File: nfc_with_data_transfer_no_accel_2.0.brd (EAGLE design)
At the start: 13.2 x 18.4 mm, 7 parts

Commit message: fixed rst
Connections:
- net DOT1: now also MCU.6; no longer MCU.2
- net DOT5: now also MCU.1; no longer MCU.6
- net RST: now also MCU.2; no longer MCU.1
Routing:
- net DOT5: track 10.3 -> 0.00 mm
- net DOT1: track 3.30 -> 10.0 mm
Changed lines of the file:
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@@
 <layer number="14" name="Route14" color="1" fill="6" visible="no" active="no"/>
 <layer number="15" name="Route15" color="4" fill="6" visible="no" active="no"/>
-<layer number="16" name="Bottom" color="1" fill="1" visible="yes" active="yes"/>
+<layer number="16" name="Bottom" color="1" fill="1" visible="no" active="yes"/>
 <layer number="17" name="Pads" color="2" fill="1" visible="yes" active="yes"/>
 <layer number="18" name="Vias" color="2" fill="1" visible="yes" active="yes"/>
@@
 <contactref element="EINK" pad="5"/>
 <contactref element="MCU" pad="3"/>
+<wire x1="7.5946" y1="10.4394" x2="7.747" y2="10.287" width="0.3048" layer="1"/>
 <wire x1="8.5344" y1="7.6454" x2="8.5344" y2="8.6106" width="0.3048" layer="1"/>
-<wire x1="8.5344" y1="8.6106" x2="7.747" y2="9.398" width="0.3048" layer="1"/>
-<wire x1="7.747" y1="9.398" x2="7.747" y2="10.287" width="0.3048" layer="1"/>
-<wire x1="7.747" y1="10.287" x2="7.5946" y2="10.4394" width="0.3048" layer="1"/>
+<wire x1="8.5344" y1="8.6106" x2="7.62" y2="9.525" width="0.3048" layer="1"/>
+<wire x1="7.62" y1="9.525" x2="7.62" y2="10.414" width="0.3048" layer="1"/>
+<wire x1="7.62" y1="10.414" x2="7.5946" y2="10.4394" width="0.3048" layer="1"/>
 </signal>
 <signal name="DOT1">
 <contactref element="EINK" pad="3"/>
-<contactref element="MCU" pad="2"/>
-<wire x1="7.5438" y1="7.6454" x2="7.5438" y2="8.4582" width="0.3048" layer="1"/>
-<wire x1="7.5438" y1="8.4582" x2="6.35" y2="9.652" width="0.3048" layer="1"/>
-<wire x1="6.35" y1="9.652" x2="6.35" y2="10.414" width="0.3048" layer="1"/>
-<wire x1="6.35" y1="10.414" x2="6.3246" y2="10.4394" width="0.3048" layer="1"/>
+<contactref element="MCU" pad="6"/>
+<wire x1="7.5438" y1="7.6454" x2="7.5438" y2="8.3312" width="0.3048" layer="1"/>
+<wire x1="7.5438" y1="8.3312" x2="6.985" y2="8.89" width="0.3048" layer="1"/>
+<wire x1="6.985" y1="8.89" x2="6.985" y2="15.24" width="0.3048" layer="1"/>
+<wire x1="6.985" y1="15.24" x2="7.62" y2="15.875" width="0.3048" layer="1"/>
+<wire x1="7.62" y1="15.875" x2="7.62" y2="17.145" width="0.3048" layer="1"/>
+<wire x1="7.62" y1="17.145" x2="7.5946" y2="17.1704" width="0.3048" layer="1"/>
 </signal>
 <signal name="RST">
 <contactref element="EINK" pad="1"/>
-<contactref element="MCU" pad="1"/>
 <wire x1="6.5278" y1="7.9502" x2="6.5278" y2="7.6454" width="0.3048" layer="1"/>
-<wire x1="6.5278" y1="7.6454" x2="6.5278" y2="8.0772" width="0.3048" layer="1"/>
 <wire x1="5.08" y1="9.525" x2="5.08" y2="10.414" width="0.3048" layer="1"/>
-<wire x1="5.08" y1="10.414" x2="5.0546" y2="10.4394" width="0.3048" layer="1"/>
-<wire x1="6.5278" y1="7.6454" x2="6.5278" y2="8.0772" width="0.3048" layer="1"/>
-<wire x1="6.5278" y1="8.0772" x2="5.08" y2="9.525" width="0.3048" layer="1"/>
+<contactref element="MCU" pad="2"/>
+<wire x1="6.5278" y1="7.6454" x2="6.5278" y2="10.2362" width="0.3048" layer="1"/>
+<wire x1="6.5278" y1="10.2362" x2="6.3246" y2="10.4394" width="0.3048" layer="1"/>
+<wire x1="6.3246" y1="10.4394" x2="5.08" y2="10.414" width="0" layer="19" extent="1-1"/>
 </signal>
 <signal name="2.8V">
@@
 <signal name="DOT5">
 <contactref element="EINK" pad="7"/>
-<contactref element="MCU" pad="6"/>
-<wire x1="9.525" y1="11.557" x2="9.525" y2="7.6454" width="0.3048" layer="1"/>
-<wire x1="7.5946" y1="17.1704" x2="7.5946" y2="13.4874" width="0.3048" layer="1"/>
-<wire x1="7.5946" y1="13.4874" x2="9.525" y2="11.557" width="0.3048" layer="1"/>
+<contactref element="MCU" pad="1"/>
+<wire x1="5.0546" y1="10.4394" x2="9.525" y2="7.6454" width="0" layer="19" extent="1-1"/>
 </signal>
 </signals>

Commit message: final
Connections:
- removed net DOT3: EINK.5, MCU.3
- net DOT1: now also MCU.3; no longer MCU.6
- net DOT5: now also MCU.6; no longer MCU.1
- net GND: now also EINK.5
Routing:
- net GND: track 18.5 -> 32.1 mm
- net DOT5: track 0.00 -> 10.3 mm
- net DOT1: track 10.0 -> 2.82 mm
- net DOT3: track 3.40 -> 0.00 mm
- net RST: track 4.07 -> 3.18 mm
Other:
- board text added: "AlterNail"
- board text added: "RevB"
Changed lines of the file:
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@@
 <dimension x1="16.891" y1="2.032128125" x2="16.891" y2="20.32" x3="20.828" y3="11.1760625" textsize="1.778" layer="47"/>
 <dimension x1="16.891" y1="20.32" x2="3.683" y2="20.32" x3="10.287" y3="22.225" textsize="1.778" layer="47"/>
+<text x="11.557" y="6.096" size="1.27" layer="16" font="vector" ratio="20" rot="MR90">AlterNail</text>
+<text x="9.271" y="6.223" size="1.27" layer="16" font="vector" ratio="20" rot="MR90">RevB</text>
 </plain>
 <attributes>
@@
 </elements>
 <signals>
-<signal name="DOT3">
-<contactref element="EINK" pad="5"/>
-<contactref element="MCU" pad="3"/>
-<wire x1="7.5946" y1="10.4394" x2="7.747" y2="10.287" width="0.3048" layer="1"/>
-<wire x1="8.5344" y1="7.6454" x2="8.5344" y2="8.6106" width="0.3048" layer="1"/>
-<wire x1="8.5344" y1="8.6106" x2="7.62" y2="9.525" width="0.3048" layer="1"/>
-<wire x1="7.62" y1="9.525" x2="7.62" y2="10.414" width="0.3048" layer="1"/>
-<wire x1="7.62" y1="10.414" x2="7.5946" y2="10.4394" width="0.3048" layer="1"/>
-</signal>
 <signal name="DOT1">
 <contactref element="EINK" pad="3"/>
-<contactref element="MCU" pad="6"/>
-<wire x1="7.5438" y1="7.6454" x2="7.5438" y2="8.3312" width="0.3048" layer="1"/>
-<wire x1="7.5438" y1="8.3312" x2="6.985" y2="8.89" width="0.3048" layer="1"/>
-<wire x1="6.985" y1="8.89" x2="6.985" y2="15.24" width="0.3048" layer="1"/>
-<wire x1="6.985" y1="15.24" x2="7.62" y2="15.875" width="0.3048" layer="1"/>
-<wire x1="7.62" y1="15.875" x2="7.62" y2="17.145" width="0.3048" layer="1"/>
-<wire x1="7.62" y1="17.145" x2="7.5946" y2="17.1704" width="0.3048" layer="1"/>
+<contactref element="MCU" pad="3"/>
+<wire x1="7.5438" y1="7.6454" x2="7.5438" y2="10.3886" width="0.3048" layer="1"/>
+<wire x1="7.5438" y1="10.3886" x2="7.5946" y2="10.4394" width="0.3048" layer="1"/>
 </signal>
 <signal name="RST">
 <contactref element="EINK" pad="1"/>
 <wire x1="6.5278" y1="7.9502" x2="6.5278" y2="7.6454" width="0.3048" layer="1"/>
-<wire x1="5.08" y1="9.525" x2="5.08" y2="10.414" width="0.3048" layer="1"/>
 <contactref element="MCU" pad="2"/>
-<wire x1="6.5278" y1="7.6454" x2="6.5278" y2="10.2362" width="0.3048" layer="1"/>
-<wire x1="6.5278" y1="10.2362" x2="6.3246" y2="10.4394" width="0.3048" layer="1"/>
-<wire x1="6.3246" y1="10.4394" x2="5.08" y2="10.414" width="0" layer="19" extent="1-1"/>
+<wire x1="6.5278" y1="7.6454" x2="6.5278" y2="8.7122" width="0.3048" layer="1"/>
+<wire x1="6.5278" y1="8.7122" x2="6.35" y2="8.89" width="0.3048" layer="1"/>
+<wire x1="6.35" y1="8.89" x2="6.35" y2="10.414" width="0.3048" layer="1"/>
+<wire x1="6.35" y1="10.414" x2="6.3246" y2="10.4394" width="0.3048" layer="1"/>
 </signal>
 <signal name="2.8V">
@@
 <contactref element="C1" pad="1"/>
 <wire x1="15.3322" y1="13.5434" x2="15.3322" y2="14.1934" width="0.3048" layer="1"/>
-<wire x1="15.3322" y1="13.5434" x2="15.9206" y2="13.5434" width="0.3048" layer="1"/>
-<wire x1="15.9206" y1="13.5434" x2="16.383" y2="13.081" width="0.3048" layer="1"/>
-<wire x1="16.383" y1="13.081" x2="16.383" y2="10.795" width="0.3048" layer="1"/>
-<wire x1="16.383" y1="10.795" x2="15.113" y2="9.525" width="0.3048" layer="1"/>
+<wire x1="15.3322" y1="13.5434" x2="15.7936" y2="13.5434" width="0.3048" layer="1"/>
+<wire x1="15.7936" y1="13.5434" x2="16.002" y2="13.335" width="0.3048" layer="1"/>
+<wire x1="16.002" y1="13.335" x2="16.002" y2="10.414" width="0.3048" layer="1"/>
+<wire x1="16.002" y1="10.414" x2="15.113" y2="9.525" width="0.3048" layer="1"/>
 <wire x1="15.113" y1="9.525" x2="14.6186" y2="9.525" width="0.3048" layer="1"/>
 <wire x1="14.6186" y1="9.525" x2="14.5288" y2="9.6148" width="0.3048" layer="1"/>
@@
 <contactref element="R5" pad="1"/>
 <wire x1="12.827" y1="11.3148" x2="12.7" y2="11.176" width="0.3048" layer="1"/>
-<wire x1="11.4756" y1="13.5434" x2="10.9822" y2="13.5434" width="0.3048" layer="1"/>
 <wire x1="11.4756" y1="13.5434" x2="12.827" y2="12.192" width="0.3048" layer="1"/>
 <wire x1="12.827" y1="12.192" x2="12.827" y2="11.3148" width="0.3048" layer="1"/>
-<wire x1="6.3246" y1="17.1704" x2="6.3246" y2="18.2626" width="0.3048" layer="1"/>
-<wire x1="6.3246" y1="18.2626" x2="6.604" y2="18.542" width="0.3048" layer="1"/>
-<wire x1="8.2296" y1="18.288" x2="8.2296" y2="15.24" width="0.3048" layer="1"/>
+<wire x1="6.3246" y1="17.1704" x2="6.3246" y2="18.288" width="0.3048" layer="1"/>
+<wire x1="6.3246" y1="18.288" x2="6.604" y2="18.5928" width="0.3048" layer="1"/>
+<wire x1="8.2296" y1="15.24" x2="8.2296" y2="18.3134" width="0.3048" layer="1"/>
+<wire x1="6.604" y1="18.5928" x2="7.9502" y2="18.5928" width="0.3048" layer="1"/>
+<wire x1="7.9502" y1="18.5928" x2="8.2296" y2="18.3134" width="0.3048" layer="1"/>
 <wire x1="10.9822" y1="13.5434" x2="9.9516" y2="13.5434" width="0.3048" layer="1"/>
-<wire x1="9.9516" y1="13.5434" x2="8.2296" y2="15.24" width="0.3048" layer="1"/>
-<wire x1="6.604" y1="18.542" x2="7.9756" y2="18.542" width="0.3048" layer="1"/>
-<wire x1="7.9756" y1="18.542" x2="8.2296" y2="18.288" width="0.3048" layer="1"/>
+<wire x1="11.4756" y1="13.5434" x2="10.9822" y2="13.5434" width="0.3048" layer="1"/>
+<wire x1="8.2296" y1="15.24" x2="9.9516" y2="13.5434" width="0.3048" layer="1"/>
 </signal>
 <signal name="COIL">
@@
 <contactref element="MCU" pad="4"/>
 <contactref element="C1" pad="2"/>
-<polygon width="0.3048" layer="1">
+<polygon width="0.3048" layer="1" rank="2">
 <vertex x="17.653" y="19.558"/>
 <vertex x="3.048" y="19.558"/>
@@
 <vertex x="17.653" y="2.286"/>
 </polygon>
-<wire x1="8.0264" y1="6.7056" x2="8.0264" y2="7.6454" width="0.3048" layer="1"/>
-<wire x1="8.0264" y1="6.7056" x2="8.128" y2="6.604" width="0.3048" layer="1"/>
-<wire x1="9.0424" y1="6.6294" x2="9.0424" y2="7.6454" width="0.3048" layer="1"/>
-<wire x1="9.0424" y1="6.6294" x2="9.017" y2="6.604" width="0.3048" layer="1"/>
 <wire x1="11.4524" y1="17.7038" x2="10.9982" y2="17.7038" width="0.3048" layer="1"/>
 <wire x1="10.9982" y1="17.7038" x2="9.525" y2="19.05" width="0.3048" layer="1"/>
 <wire x1="9.525" y1="19.05" x2="6.223" y2="19.05" width="0.3048" layer="1"/>
-<wire x1="6.223" y1="19.05" x2="5.715" y2="18.542" width="0.3048" layer="1"/>
-<wire x1="5.715" y1="18.542" x2="5.715" y2="15.367" width="0.3048" layer="1"/>
-<wire x1="5.715" y1="15.367" x2="5.588" y2="15.24" width="0.3048" layer="1"/>
+<wire x1="6.223" y1="19.05" x2="5.6896" y2="18.4912" width="0.3048" layer="1"/>
+<wire x1="5.6896" y1="18.4912" x2="5.6896" y2="15.3162" width="0.3048" layer="1"/>
+<wire x1="5.6896" y1="15.3162" x2="5.588" y2="15.24" width="0.3048" layer="1"/>
 <wire x1="10.9822" y1="14.1934" x2="10.5716" y2="14.1934" width="0.3048" layer="1"/>
 <wire x1="10.5716" y1="14.1934" x2="9.906" y2="14.859" width="0.3048" layer="1"/>
@@
 <wire x1="9.906" y1="14.859" x2="9.906" y2="12.573" width="0.3048" layer="16"/>
 <via x="9.906" y="12.573" extent="1-16" drill="0.6" shape="octagon"/>
-<wire x1="9.0424" y1="7.6454" x2="9.0424" y2="10.2616" width="0.3048" layer="1"/>
-<wire x1="9.0424" y1="10.2616" x2="8.8646" y2="10.4394" width="0.3048" layer="1"/>
-<wire x1="10.9982" y1="17.7038" x2="9.906" y2="14.859" width="0" layer="19" extent="1-1"/>
+<contactref element="EINK" pad="5"/>
+<wire x1="9.0424" y1="6.4516" x2="8.5344" y2="6.4516" width="0.3048" layer="1"/>
+<wire x1="8.0264" y1="6.5278" x2="8.0264" y2="7.6454" width="0.3048" layer="1"/>
+<wire x1="8.0264" y1="6.5278" x2="8.5344" y2="6.5278" width="0.3048" layer="1"/>
+<wire x1="8.5344" y1="6.5278" x2="8.5344" y2="6.4516" width="0.3048" layer="1"/>
+<wire x1="8.5344" y1="8.7376" x2="8.5344" y2="6.5278" width="0.3048" layer="1"/>
+<wire x1="8.5344" y1="8.7376" x2="9.0424" y2="8.7376" width="0.3048" layer="1"/>
+<wire x1="9.0424" y1="8.7376" x2="9.0424" y2="8.763" width="0.3048" layer="1"/>
+<wire x1="9.0424" y1="8.7376" x2="9.0424" y2="7.6454" width="0.3048" layer="1"/>
+<wire x1="9.0424" y1="7.6454" x2="9.0424" y2="6.4516" width="0.3048" layer="1"/>
+<wire x1="8.0264" y1="7.6454" x2="8.0264" y2="8.8392" width="0.3048" layer="1"/>
+<wire x1="8.0264" y1="8.8392" x2="8.5344" y2="8.8392" width="0.3048" layer="1"/>
+<wire x1="8.5344" y1="8.8392" x2="8.5344" y2="8.7376" width="0.3048" layer="1"/>
+<wire x1="7.0358" y1="7.6454" x2="7.0358" y2="8.9916" width="0.3048" layer="1"/>
+<wire x1="7.0358" y1="8.9916" x2="6.9596" y2="9.0678" width="0.3048" layer="1"/>
+<wire x1="6.9596" y1="9.0678" x2="6.9596" y2="12.0396" width="0.3048" layer="1"/>
+<wire x1="6.9596" y1="12.0396" x2="5.715" y2="12.0396" width="0.3048" layer="1"/>
+<wire x1="5.715" y1="12.0396" x2="5.6896" y2="12.065" width="0.3048" layer="1"/>
+<wire x1="5.6896" y1="12.065" x2="5.6896" y2="8.3312" width="0.3048" layer="1"/>
+<wire x1="5.6896" y1="8.3312" x2="5.588" y2="8.2296" width="0.3048" layer="1"/>
 </signal>
 <signal name="FD">
@@
 <signal name="DOT5">
 <contactref element="EINK" pad="7"/>
-<contactref element="MCU" pad="1"/>
-<wire x1="5.0546" y1="10.4394" x2="9.525" y2="7.6454" width="0" layer="19" extent="1-1"/>
+<contactref element="MCU" pad="6"/>
+<wire x1="7.5946" y1="13.6144" x2="7.5946" y2="17.1704" width="0.3048" layer="1"/>
+<wire x1="9.525" y1="11.684" x2="7.5946" y2="13.6144" width="0.3048" layer="1"/>
+<wire x1="9.525" y1="7.6454" x2="9.525" y2="11.684" width="0.3048" layer="1"/>
 </signal>
 </signals>

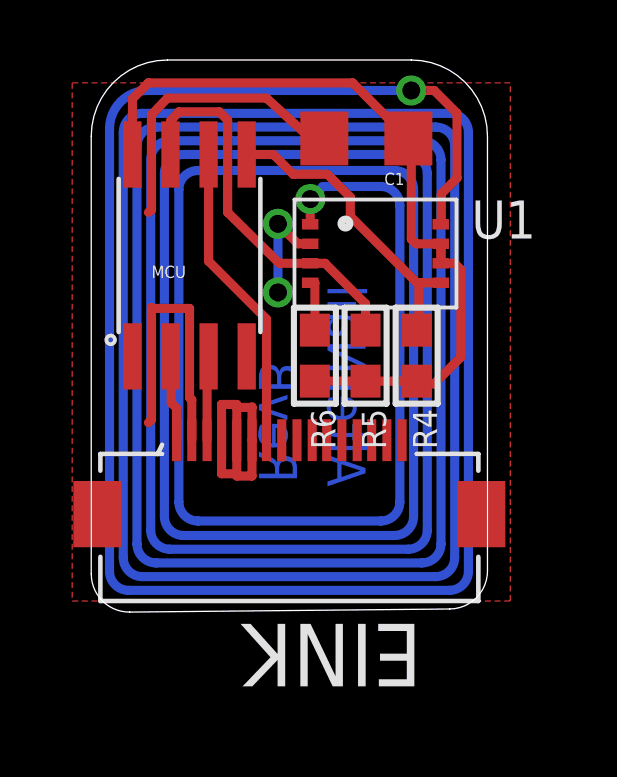
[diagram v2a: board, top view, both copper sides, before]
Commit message: latest without top ground plane
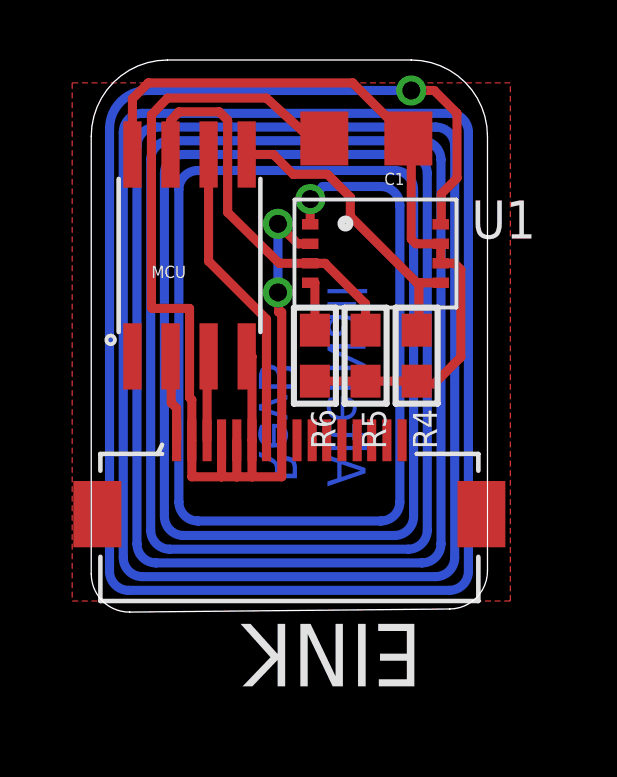
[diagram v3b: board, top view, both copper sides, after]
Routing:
- net GND: track 32.1 -> 39.4 mm

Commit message: Tweaks by Eric to produce first manufactured board
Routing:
- removed copper zone on layer 1, net GND
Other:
- board size 13.2 x 18.4 mm -> 15.2 x 18.1 mm
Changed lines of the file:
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@@
 <?xml version="1.0" encoding="utf-8"?>
 <!DOCTYPE eagle SYSTEM "eagle.dtd">
-<eagle version="7.6.0">
+<eagle version="8.2.1">
 <drawing>
 <settings>
@@
 <setting verticaltext="up"/>
 </settings>
-<grid distance="0.001" unitdist="inch" unit="inch" style="lines" multiple="1" display="yes" altdistance="0.001" altunitdist="inch" altunit="inch"/>
+<grid distance="0.001" unitdist="inch" unit="mil" style="lines" multiple="1" display="yes" altdistance="0.001" altunitdist="inch" altunit="inch"/>
 <layers>
 <layer number="1" name="Top" color="4" fill="1" visible="yes" active="yes"/>
@@
 <layer number="15" name="Route15" color="4" fill="6" visible="no" active="no"/>
 <layer number="16" name="Bottom" color="1" fill="1" visible="yes" active="yes"/>
-<layer number="17" name="Pads" color="2" fill="1" visible="no" active="yes"/>
+<layer number="17" name="Pads" color="2" fill="1" visible="yes" active="yes"/>
 <layer number="18" name="Vias" color="2" fill="1" visible="yes" active="yes"/>
 <layer number="19" name="Unrouted" color="6" fill="1" visible="yes" active="yes"/>
 <layer number="20" name="Dimension" color="15" fill="1" visible="yes" active="yes"/>
-<layer number="21" name="tPlace" color="7" fill="1" visible="yes" active="yes"/>
+<layer number="21" name="tPlace" color="7" fill="1" visible="no" active="yes"/>
 <layer number="22" name="bPlace" color="7" fill="1" visible="no" active="yes"/>
 <layer number="23" name="tOrigins" color="15" fill="1" visible="no" active="yes"/>
 <layer number="24" name="bOrigins" color="15" fill="1" visible="no" active="yes"/>
 <layer number="25" name="tNames" color="7" fill="1" visible="no" active="yes"/>
-<layer number="26" name="bNames" color="7" fill="1" visible="no" active="yes"/>
+<layer number="26" name="bNames" color="7" fill="1" visible="yes" active="yes"/>
 <layer number="27" name="tValues" color="7" fill="1" visible="no" active="yes"/>
 <layer number="28" name="bValues" color="7" fill="1" visible="no" active="yes"/>
@@
 <layer number="131" name="tAdjust" color="7" fill="1" visible="no" active="yes"/>
 <layer number="132" name="bAdjust" color="7" fill="1" visible="no" active="yes"/>
-<layer number="144" name="Drill_legend" color="7" fill="1" visible="no" active="yes"/>
+<layer number="144" name="Drill_legend" color="7" fill="1" visible="yes" active="yes"/>
 <layer number="150" name="Notes" color="7" fill="1" visible="no" active="yes"/>
 <layer number="151" name="HeatSink" color="7" fill="1" visible="no" active="yes"/>
@@
 <board>
 <plain>
-<wire x1="3.683" y1="17.78" x2="3.683" y2="3.18728125" width="0" layer="20"/>
-<wire x1="3.683" y1="3.18728125" x2="4.965221875" y2="1.917340625" width="0" layer="20" curve="90.551396"/>
-<wire x1="4.965221875" y1="1.917340625" x2="15.633221875" y2="2.020021875" width="0" layer="20"/>
-<wire x1="15.633221875" y1="2.020021875" x2="16.891" y2="3.2899625" width="0" layer="20" curve="89.455027"/>
-<wire x1="16.891" y1="3.2899625" x2="16.891" y2="17.78" width="0" layer="20"/>
-<wire x1="16.891" y1="17.78" x2="14.351" y2="20.32" width="0" layer="20" curve="90"/>
-<wire x1="14.351" y1="20.32" x2="6.223" y2="20.32" width="0" layer="20"/>
-<wire x1="6.223" y1="20.32" x2="3.683" y2="17.78" width="0" layer="20" curve="90"/>
 <dimension x1="16.891" y1="2.032128125" x2="16.891" y2="20.32" x3="20.828" y3="11.1760625" textsize="1.778" layer="47"/>
 <dimension x1="16.891" y1="20.32" x2="3.683" y2="20.32" x3="10.287" y3="22.225" textsize="1.778" layer="47"/>
-<text x="11.557" y="6.096" size="1.27" layer="16" font="vector" ratio="20" rot="MR90">AlterNail</text>
-<text x="9.271" y="6.223" size="1.27" layer="16" font="vector" ratio="20" rot="MR90">RevB</text>
+<text x="11.5316" y="6.096" size="1.27" layer="26" font="vector" ratio="20" rot="MR90">AlterNail</text>
+<text x="9.271" y="6.223" size="1.27" layer="26" font="vector" ratio="20" rot="MR90">RevB</text>
+<wire x1="2.7686" y1="2.159" x2="2.7686" y2="19.9136" width="0.254" layer="20"/>
+<wire x1="2.7686" y1="19.9136" x2="2.8448" y2="19.9898" width="0.254" layer="20"/>
+<wire x1="2.8448" y1="20.0914" x2="17.907" y2="20.0914" width="0.254" layer="20"/>
+<wire x1="17.907" y1="20.0914" x2="17.9578" y2="20.0406" width="0.254" layer="20"/>
+<wire x1="17.9578" y1="20.0406" x2="17.9578" y2="2.032" width="0.254" layer="20"/>
+<wire x1="17.9578" y1="2.032" x2="17.9324" y2="2.0066" width="0.254" layer="20"/>
+<wire x1="17.9324" y1="2.0066" x2="2.8448" y2="2.0066" width="0.254" layer="20"/>
+<wire x1="2.8448" y1="2.0066" x2="2.8194" y2="2.032" width="0.254" layer="20"/>
 </plain>
 <attributes>
@@
 <elements>
 <element name="EINK" library="Molex_By_element14_Batch_1" package="MOLEX_52892-1695" value="52892-1695" x="10.287" y="10.541" rot="R180">
+<attribute name="MPN" value="52892-1695" x="10.287" y="10.541" size="1.778" layer="27" rot="R180" display="off"/>
+<attribute name="OC_FARNELL" value="1556807" x="10.287" y="10.541" size="1.778" layer="27" rot="R180" display="off"/>
+<attribute name="OC_NEWARK" value="92M6601" x="10.287" y="10.541" size="1.778" layer="27" rot="R180" display="off"/>
 <attribute name="PACKAGE" value="CONNECTOR, FPC, ZIF, 0.50MM, 16 WAY" x="10.287" y="10.541" size="1.778" layer="27" rot="R180" display="off"/>
-<attribute name="MPN" value="52892-1695" x="10.287" y="10.541" size="1.778" layer="27" rot="R180" display="off"/>
-<attribute name="OC_NEWARK" value="92M6601" x="10.287" y="10.541" size="1.778" layer="27" rot="R180" display="off"/>
-<attribute name="OC_FARNELL" value="1556807" x="10.287" y="10.541" size="1.778" layer="27" rot="R180" display="off"/>
 <attribute name="SUPPLIER" value="Molex" x="10.287" y="10.541" size="1.778" layer="27" rot="R180" display="off"/>
 </element>
@@
 <contactref element="MCU" pad="4"/>
 <contactref element="C1" pad="2"/>
-<polygon width="0.3048" layer="1" rank="2">
-<vertex x="17.653" y="19.558"/>
-<vertex x="3.048" y="19.558"/>
-<vertex x="3.048" y="2.286"/>
-<vertex x="17.653" y="2.286"/>
-</polygon>
 <wire x1="11.4524" y1="17.7038" x2="10.9982" y2="17.7038" width="0.3048" layer="1"/>
 <wire x1="10.9982" y1="17.7038" x2="9.525" y2="19.05" width="0.3048" layer="1"/>
